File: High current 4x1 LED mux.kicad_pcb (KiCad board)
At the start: 2 copper layers, 34 parts, among them J1 Barrel_Jack_Switch, J2 Conn_01x04_Female, J3 8P8C_Shielded_x4, M1 Fan_4pin, M2 Fan_4pin, M3 Fan_4pin, M4 Fan_4pin, Q1 DMN32D2LDF-7, Q2 DMN32D2LDF-7, Q3 SUM70060E, Q4 SUM70060E, Q5 SUM70060E, Q6 SUM70060E, U1 MIC4468ZWM-TR, U2 DC DC Converter

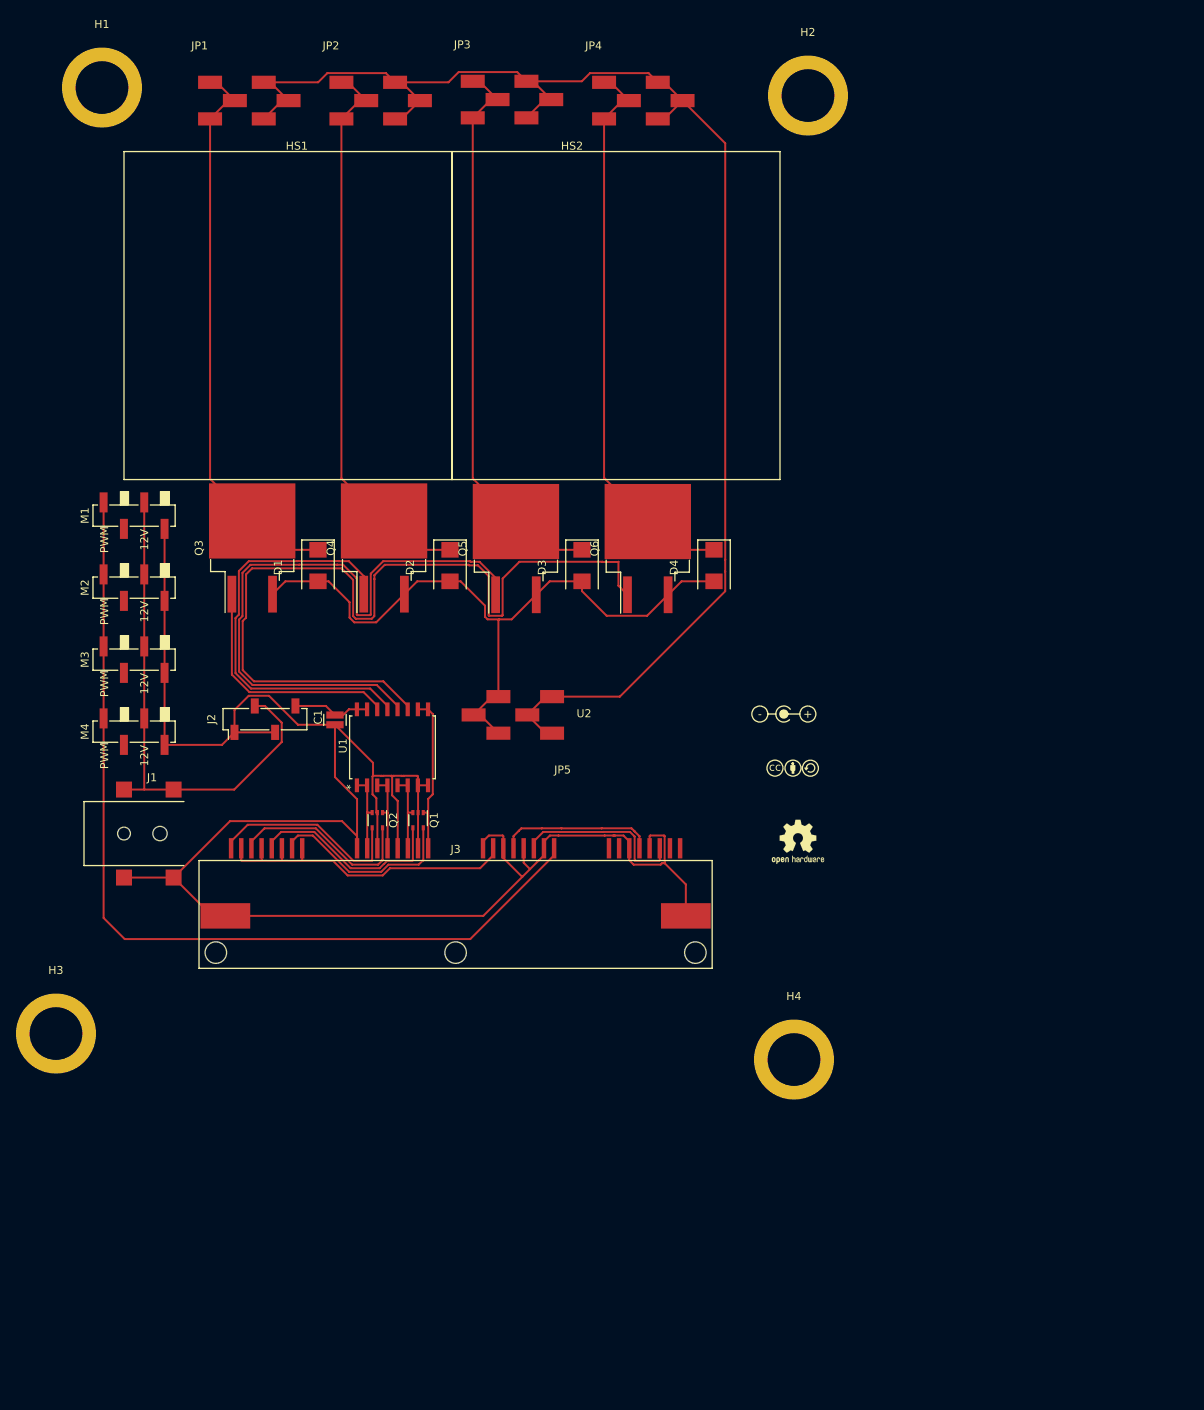
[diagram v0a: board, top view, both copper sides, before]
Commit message: Complete draft of PCB layout
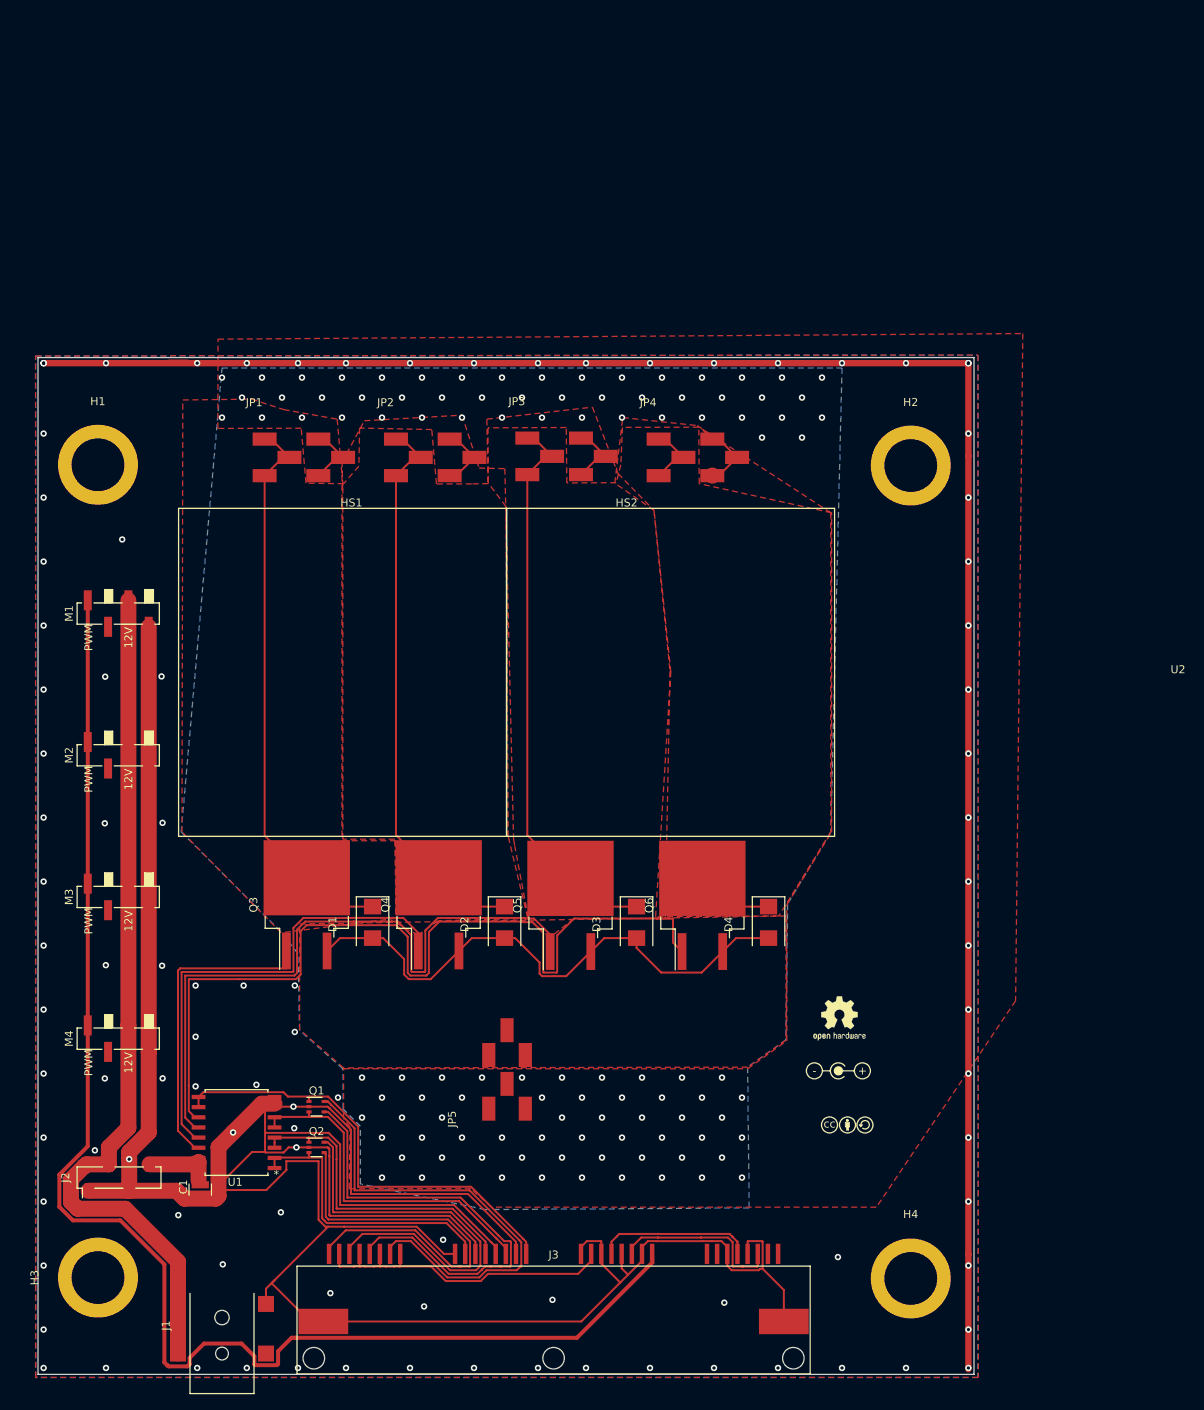
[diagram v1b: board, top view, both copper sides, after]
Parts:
- moved J1 72.1 mm to (102.5, 162.0), turned to 90 degrees
- moved C1 61.1 mm to (99.8, 136.5)
- moved J2 60.1 mm to (89.6, 135.0)
- moved J3 52.2 mm to (143.9, 143.3)
- moved U1 51.9 mm to (104.3, 129.4), turned to 180 degrees
- moved JP5 48.7 mm to (135.0, 127.9), turned to 90 degrees
- moved H2 48.0 mm to (188.6, 46.0)
- moved H1 47.2 mm to (87.0, 45.9)
- moved LOGO1 45.1 mm to (179.4, 127.3)
- moved LOGO2 45.1 mm to (179.6, 115.7)
- moved Q3 45.1 mm to (113.1, 100.9)
- moved Q4 45.1 mm to (129.6, 100.9)
- moved HS1 45.1 mm to (97.6, 51.9)
- moved HS2 45.1 mm to (138.6, 51.9)
- moved JP1 45.1 mm to (106.3, 41.9)
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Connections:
- D1 pad 1: /LED1- -> /LED4-
- D2 pad 1: /LED2- -> /LED3-
- D3 pad 1: /LED3- -> /LED2-
- D4 pad 1: /LED4- -> /LED1-
- JP1 pad 1: /LED1- -> /LED4-
- JP2 pad 1: /LED2- -> /LED3-
- JP3 pad 1: /LED3- -> /LED2-
- JP4 pad 1: /LED4- -> /LED1-
- Q3 pad 1: /Gate1 -> /Gate4
- Q3 pad 2: /LED1- -> /LED4-
- Q4 pad 1: /Gate2 -> /Gate3
- Q4 pad 2: /LED2- -> /LED3-
- Q5 pad 1: /Gate3 -> /Gate2
- Q5 pad 2: /LED3- -> /LED2-
- Q6 pad 1: /Gate4 -> /Gate1
- Q6 pad 2: /LED4- -> /LED1-
- U1 pad 11: /Gate4 -> /Gate1
- U1 pad 12: /Gate3 -> /Gate2
- U1 pad 13: /Gate2 -> /Gate3
- U1 pad 14: /Gate1 -> /Gate4
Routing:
- net GND: track 251.9 -> 669.7 mm, vias 0 -> 96
- net /LED+: track 183.2 -> 34.0 mm, vias 0 -> 105
- net /Fan_PWM: track 114.6 -> 198.6 mm
- net /Gate1: track 30.3 -> 111.3 mm
- net /12V: track 64.7 -> 134.8 mm
- net /Gate4: track 108.6 -> 39.3 mm
- net /LED1-: track 70.3 -> 17.8 mm
- net /CH1: track 19.8 -> 56.8 mm
- net /Therm1: track 24.1 -> 59.5 mm
- net /Therm2: track 25.4 -> 59.3 mm
- net /CH2: track 9.79 -> 43.6 mm
- net /Gate2: track 53.2 -> 85.6 mm
- net /CH3: track 9.80 -> 39.8 mm
- net /Therm3: track 24.1 -> 52.5 mm
- net /Therm4: track 25.4 -> 51.9 mm
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- added copper zone on B.Cu, net /LED+
- added copper zone on F.Cu, net /LED+
- added copper zone on F.Cu, net /LED-
- added copper zone on F.Cu, net /LED1-
- added copper zone on F.Cu, net /LED2-
- added copper zone on F.Cu, net /LED3-
- added copper zone on F.Cu, net /LED4-
- added copper zone on B.Cu, net GND
- added copper zone on F.Cu, net GND
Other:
- board outline added: 117 x 127.1 mm

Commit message: Add labels fix stand-off position
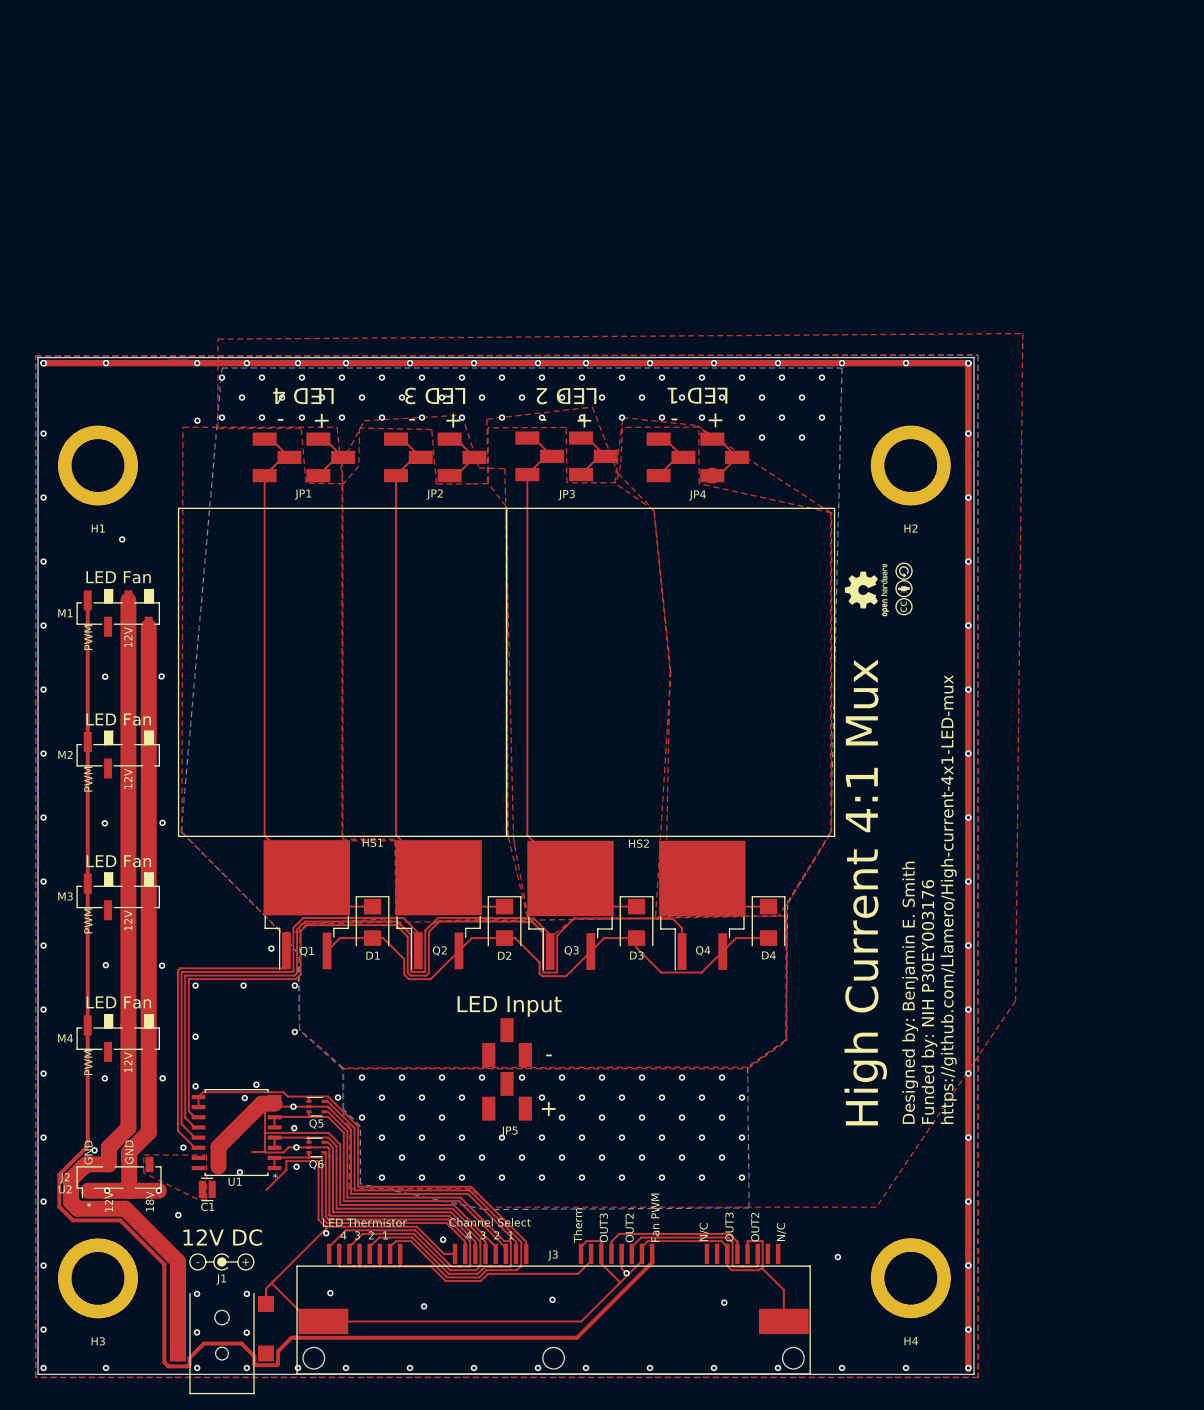
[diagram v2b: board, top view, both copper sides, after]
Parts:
- moved LOGO2 80.7 mm to (102.5, 139.6)
- moved LOGO1 65.0 mm to (186.6, 62.6), turned to 90 degrees
- moved LOGO3 53.7 mm to (183.1, 61.6), turned to 90 degrees
- moved C1 0.88 mm to (100.7, 136.5), turned to 180 degrees
- moved H1 0.10 mm to (87.0, 46.0), turned to 180 degrees
- moved H3 0.10 mm to (87.0, 147.6), turned to 180 degrees
- moved H4 0.08 mm to (188.6, 147.6), turned to 180 degrees
- turned H2 to 180 degrees
- renumbered Q3 to Q1, Q4 to Q2, Q5 to Q3, Q6 to Q4, Q1 to Q5, Q2 to Q6
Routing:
- net GND: track 669.7 -> 641.9 mm, vias 96 -> 106
- net /18V: track 9.03 -> 0.00 mm
- added copper zone on F.Cu, net /18V
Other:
- board text added: "*"
- board text added: "+"
- board text added: "+ - LED 1"
- board text added: "+ - LED 2"
- board text added: "+ - LED 3"
- board text added: "+ - LED 4"
- board text added: "-"
- board text added: "12V"
- board text added: "12V DC"
- board text added: "18V"
- board text added: "Channel Select 4 3 2 1"
- board text added: "Designed by: Benjamin E. Smith Funded by: NIH P30EY003176 https://github.com/Llamero/High-current-4x1-LED-mux"
- board text added: "GND"
- board text added: "High Current 4:1 Mux"
- board text added: "LED Fan"
- board text added: "LED Input"
- board text added: "LED Thermistor 4 3 2 1"
- board text added: "N/C OUT3 OUT2 N/C"
- board text added: "Therm OUT3 OUT2 Fan PWM"

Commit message: Add Gerber files
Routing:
- net GND: vias 106 -> 109

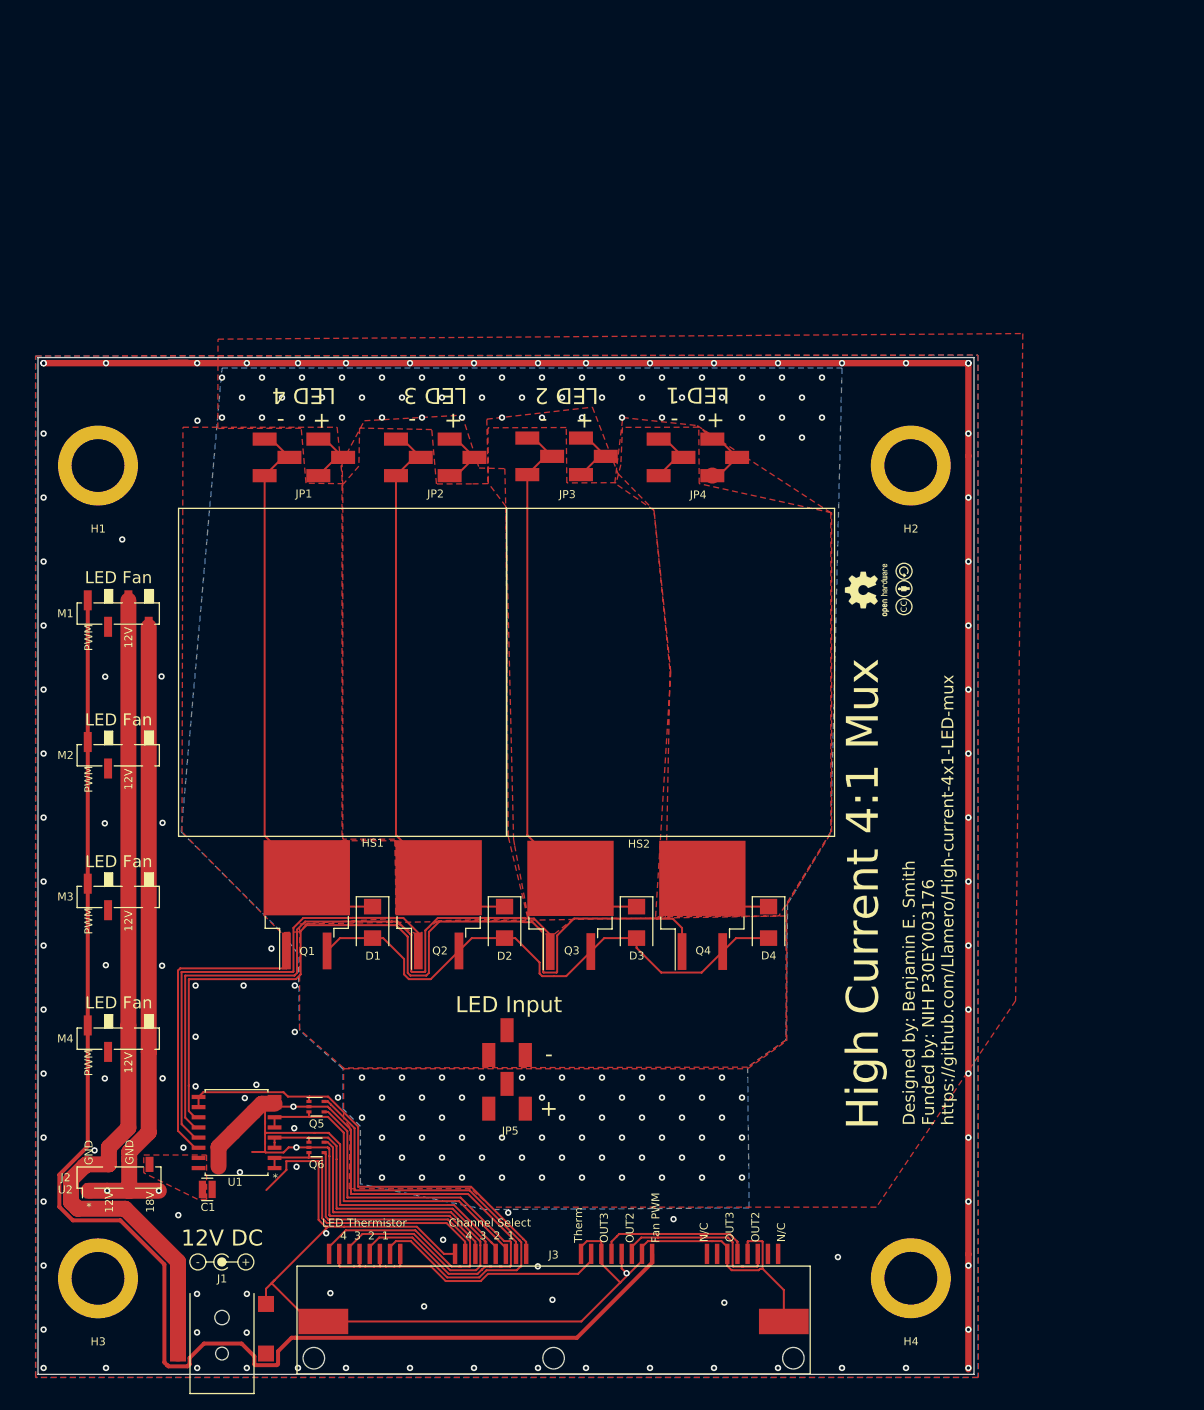
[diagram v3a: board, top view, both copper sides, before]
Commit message: Bigger spacing on 100V planes to prevent shorting
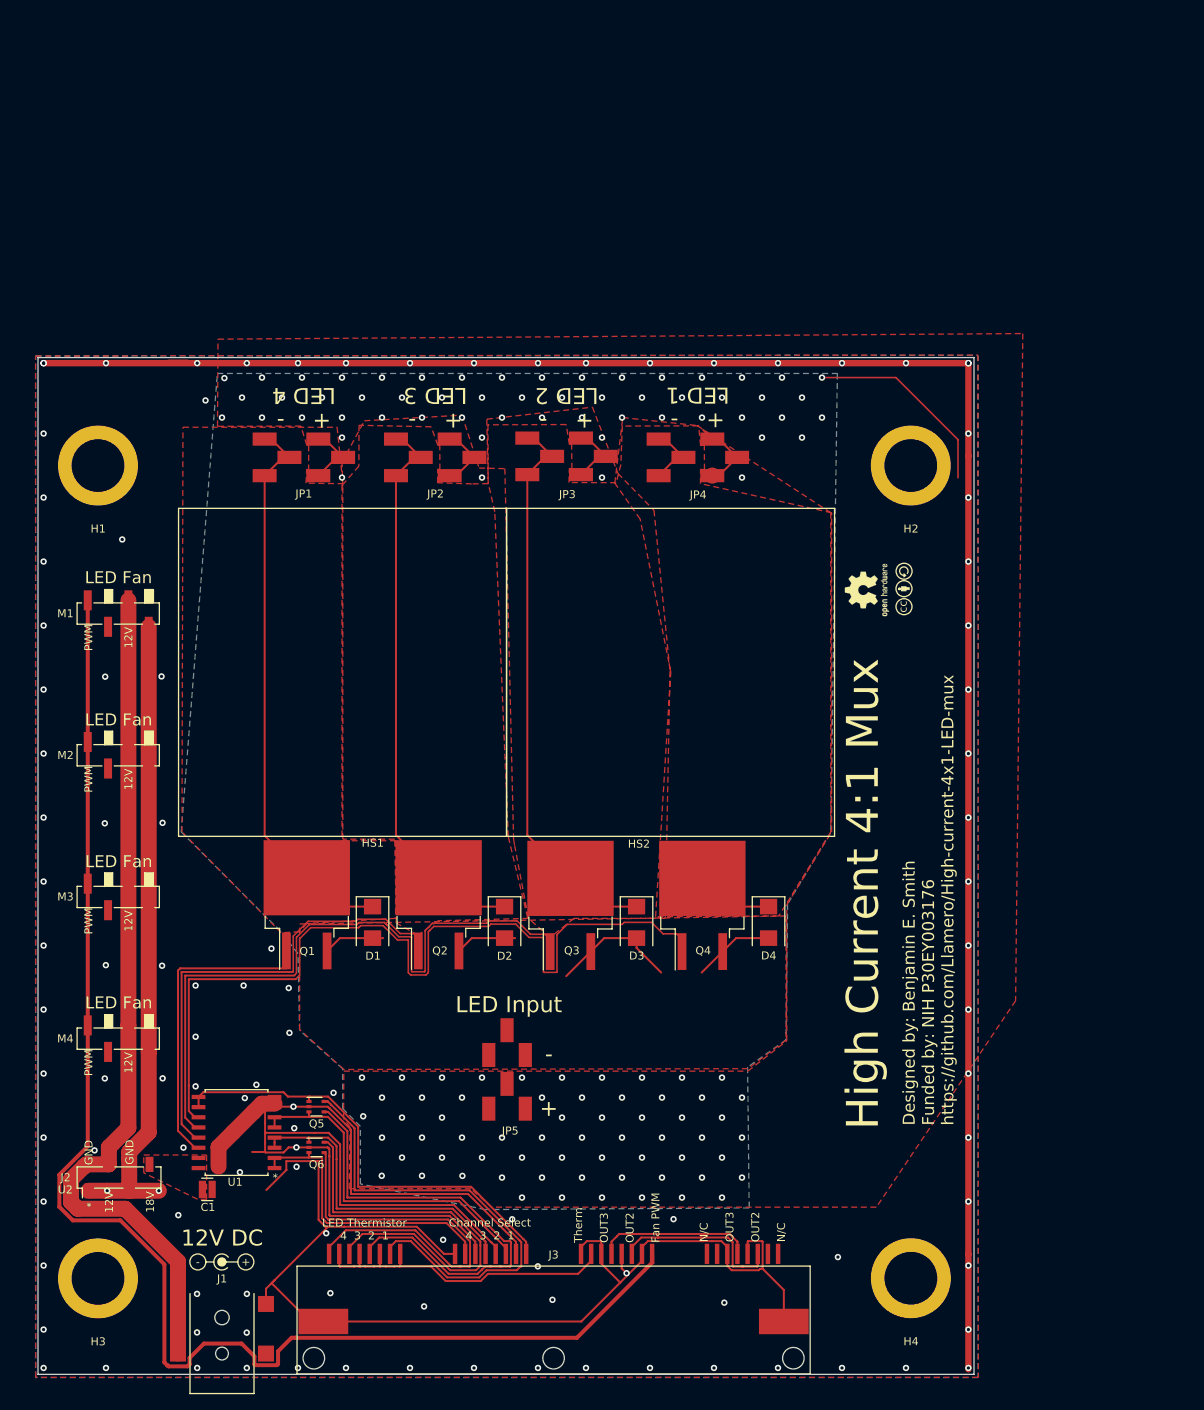
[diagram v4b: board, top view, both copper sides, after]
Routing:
- net /LED-: track 70.3 -> 41.9 mm
- net /LED+: track 34.0 -> 59.0 mm, vias 105 -> 118
- net /Gate1: track 111.3 -> 108.7 mm
- net /Gate3: track 60.5 -> 59.3 mm
- net /Gate2: track 85.6 -> 86.3 mm
